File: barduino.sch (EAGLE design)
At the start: 14 parts, among them Q2 16MHz, X1 MINI-USB-UX60A-MB-5ST

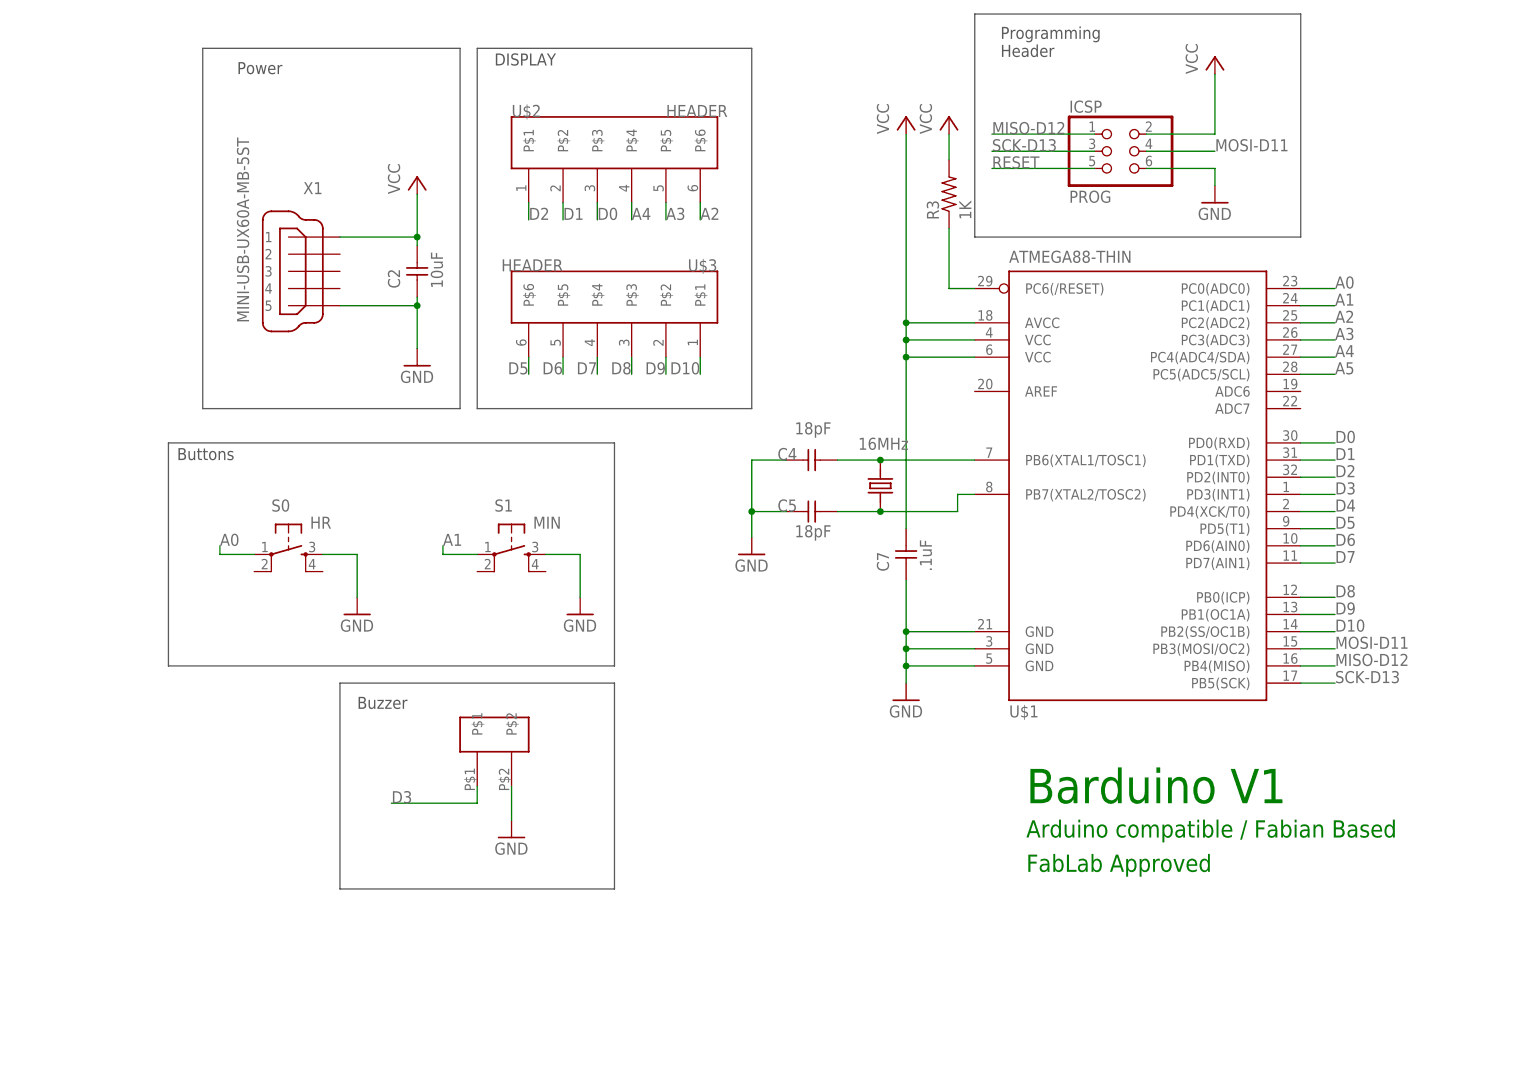
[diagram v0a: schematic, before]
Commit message: add current limiting resistors to the 4 digits
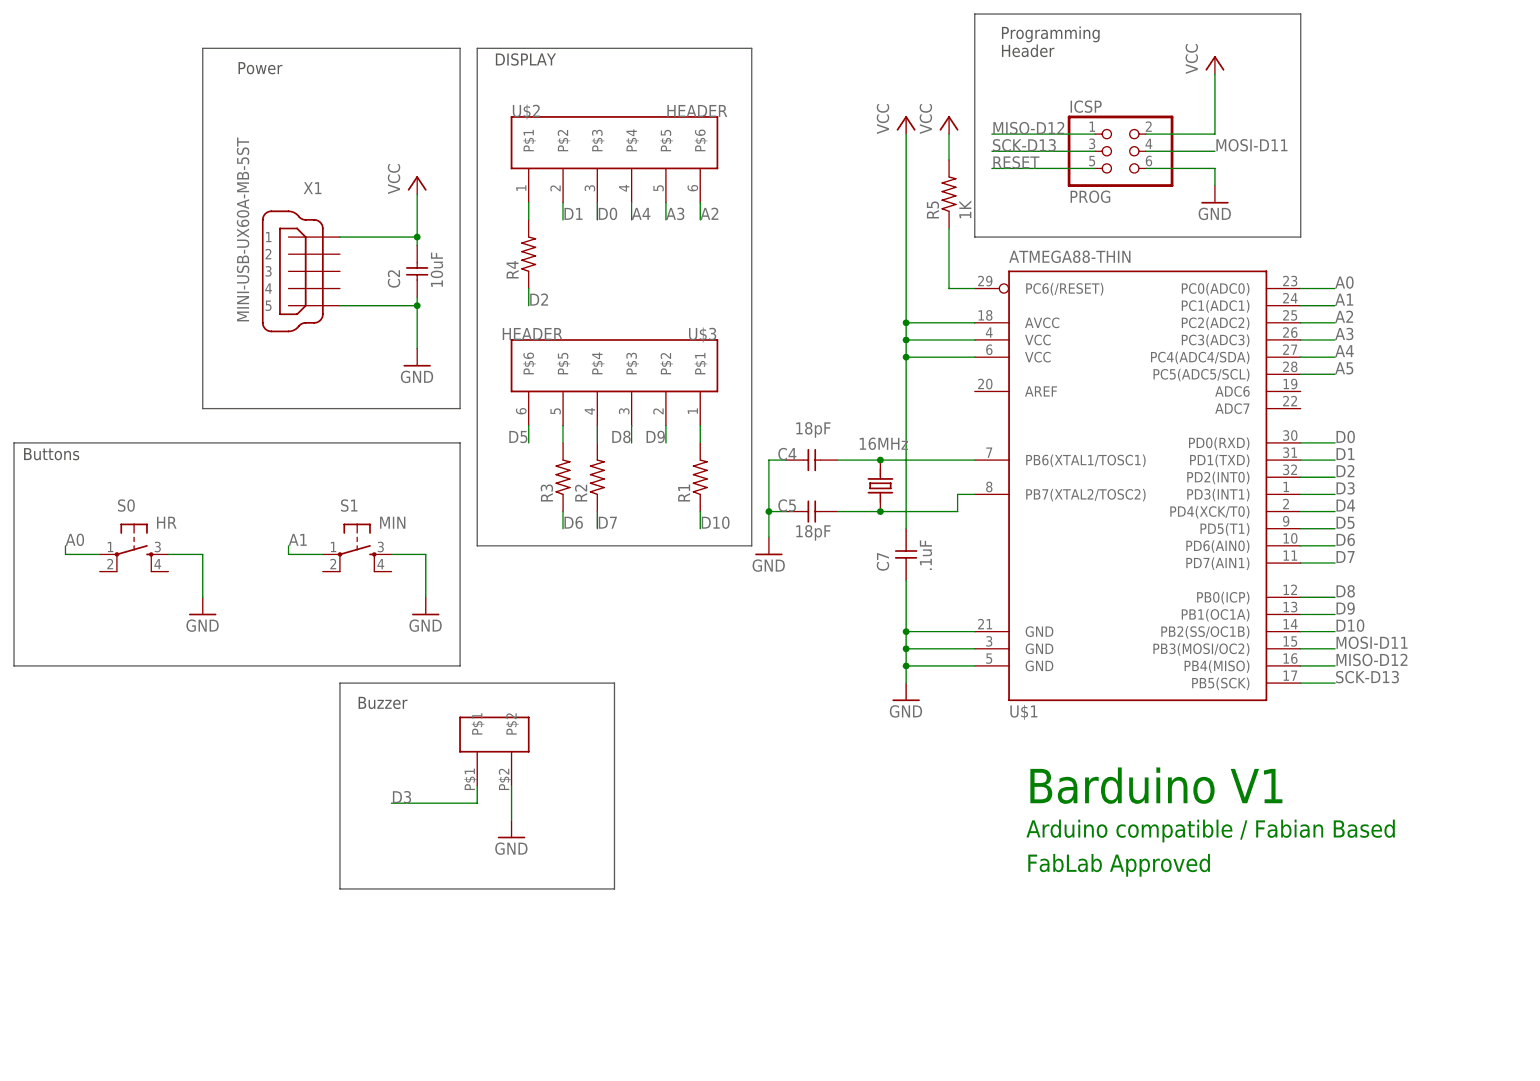
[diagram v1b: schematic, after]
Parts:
- added R1, R2, R4: (no value), resistor:R-US_R1206
- added R5: 1K, ng:RESISTOR1206
- R3: value 1K -> (none); device ng:RESISTOR1206 -> resistor:R-US_R1206
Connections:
- new net N$1: R1.2, U$3.P$1
- new net N$2: R2.2, U$3.P$4
- new net N$3: R3.2, U$3.P$5
- new net N$4: R4.2, U$2.P$1
- net D10: now also R1.1; no longer U$3.P$1
- net D2: now also R4.1; no longer U$2.P$1
- net D6: now also R3.1; no longer U$3.P$5
- net D7: now also R2.1; no longer U$3.P$4
- net RESET: now also R5.1; no longer R3.1
- net VCC: now also R5.2; no longer R3.2
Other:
- moved on the sheet: R3, S0, S1, U$3

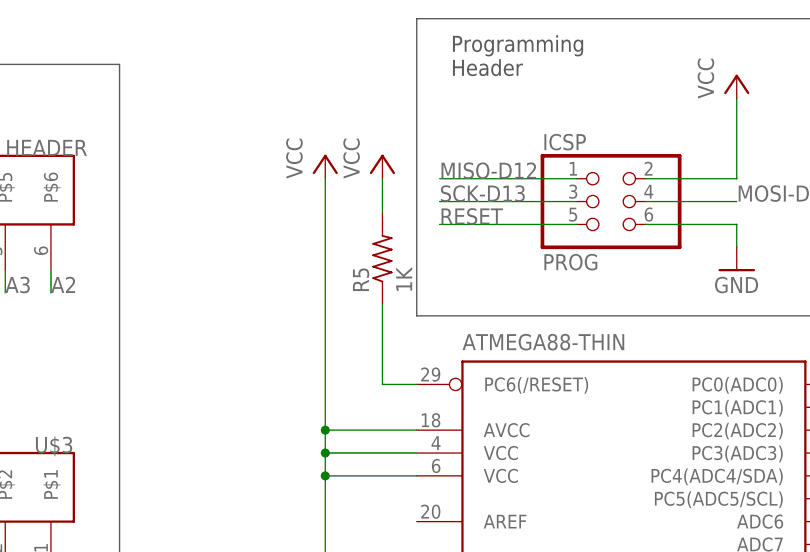
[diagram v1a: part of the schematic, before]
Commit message: reset pullup resistor should be 10k
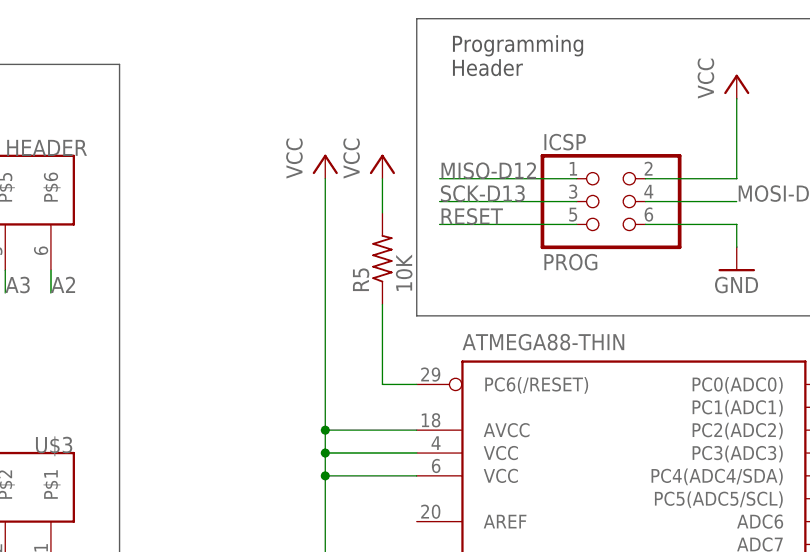
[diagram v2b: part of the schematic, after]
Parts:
- R5: value 1K -> 10K
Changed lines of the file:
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@@
 <part name="C4" library="ng" deviceset="UNPOLARIZED_CAPACITOR" device="1206" value="18pF"/>
 <part name="C5" library="ng" deviceset="UNPOLARIZED_CAPACITOR" device="1206" value="18pF"/>
-<part name="R5" library="ng" deviceset="RESISTOR" device="1206" value="1K"/>
+<part name="R5" library="ng" deviceset="RESISTOR" device="1206" value="10K"/>
 <part name="P+2" library="supply1" deviceset="VCC" device=""/>
 <part name="S0" library="ng" deviceset="6MM_SWITCH" device="6MM_SWITCH" value="HR"/>

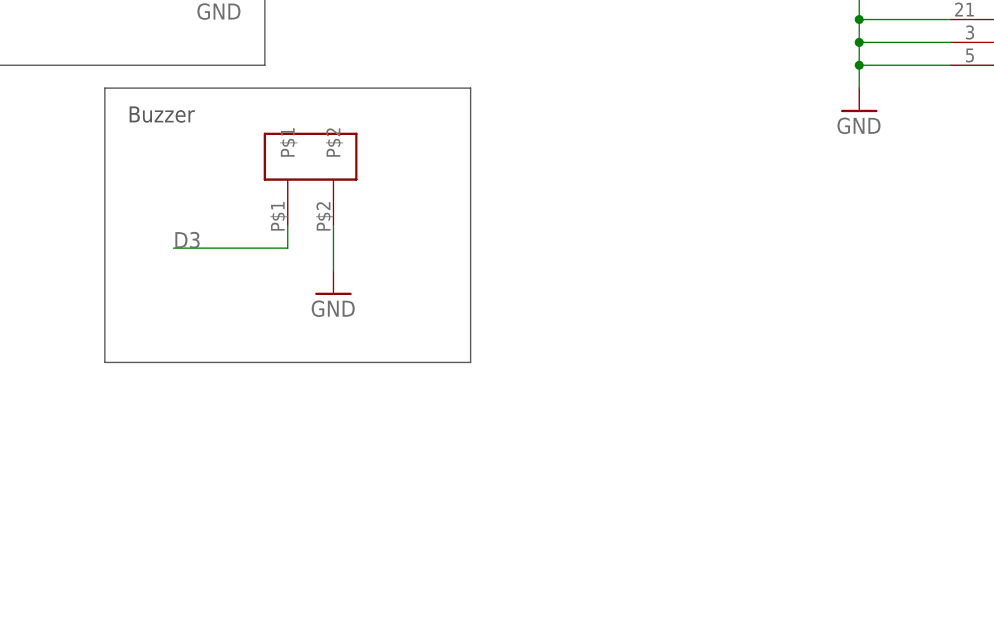
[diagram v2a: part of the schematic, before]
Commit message: add new 1206 AM and PM LEDs
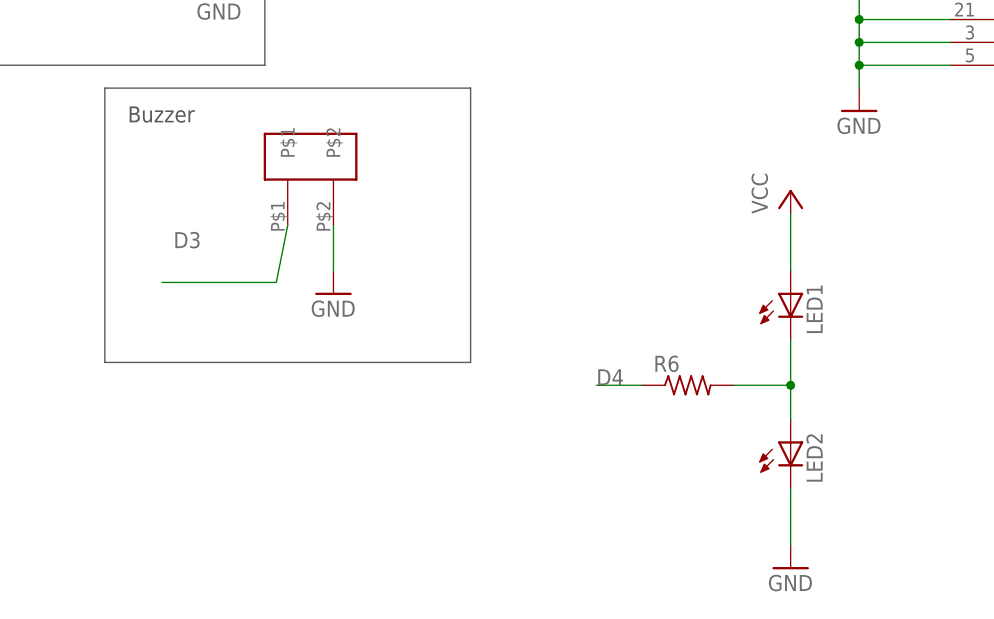
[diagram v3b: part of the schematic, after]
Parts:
- added LED1, LED2: (no value), led:LEDCHIPLED_1206
- added R6: (no value), resistor:R-US_R1206
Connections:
- new net N$5: LED1.C, LED2.A, R6.2
- net D4: now also R6.1
- net GND: now also LED2.C
- net VCC: now also LED1.A
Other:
- note added: "D4"
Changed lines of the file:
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@@
 <?xml version="1.0" encoding="utf-8"?>
 <!DOCTYPE eagle SYSTEM "eagle.dtd">
-<eagle version="8.2.1">
+<eagle version="8.2.2">
 <drawing>
 <settings>
@@
 <setting verticaltext="up"/>
 </settings>
-<grid distance="0.1" unitdist="inch" unit="inch" style="lines" multiple="1" display="no" altdistance="0.01" altunitdist="inch" altunit="inch"/>
+<grid distance="0.05" unitdist="inch" unit="inch" style="lines" multiple="1" display="no" altdistance="0.01" altunitdist="inch" altunit="inch"/>
 <layers>
 <layer number="1" name="Top" color="4" fill="1" visible="no" active="no"/>
@@
 <part name="R3" library="resistor" deviceset="R-US_" device="R1206"/>
 <part name="R4" library="resistor" deviceset="R-US_" device="R1206"/>
+<part name="LED1" library="led" deviceset="LED" device="CHIPLED_1206"/>
+<part name="LED2" library="led" deviceset="LED" device="CHIPLED_1206"/>
+<part name="P+5" library="supply1" deviceset="VCC" device=""/>
+<part name="GND8" library="supply1" library_urn="urn:adsk.eagle:library:371" deviceset="GND" device=""/>
+<part name="R6" library="resistor" deviceset="R-US_" device="R1206"/>
 </parts>
 <sheets>
@@
 <wire x1="116.84" y1="104.14" x2="116.84" y2="137.16" width="0.1524" layer="97"/>
 <wire x1="116.84" y1="137.16" x2="68.58" y2="137.16" width="0.1524" layer="97"/>
+<text x="29.21" y="5.08" size="1.778" layer="95">D4</text>
 </plain>
 <instances>
@@
 <instance part="R3" gate="G$1" x="7.62" y="68.58" rot="R90"/>
 <instance part="R4" gate="G$1" x="2.54" y="101.6" rot="R90"/>
+<instance part="LED1" gate="G$1" x="50.8" y="15.24"/>
+<instance part="LED2" gate="G$1" x="50.8" y="-1.27"/>
+<instance part="P+5" gate="VCC" x="50.8" y="26.67"/>
+<instance part="GND8" gate="1" x="50.8" y="-15.24"/>
+<instance part="R6" gate="G$1" x="39.37" y="5.08"/>
 </instances>
 <busses>
@@
 <pinref part="P+1" gate="VCC" pin="VCC"/>
 </segment>
+<segment>
+<wire x1="50.8" y1="24.13" x2="50.8" y2="17.78" width="0.1524" layer="91"/>
+<pinref part="P+5" gate="VCC" pin="VCC"/>
+<pinref part="LED1" gate="G$1" pin="A"/>
+</segment>
 </net>
 <net name="GND" class="1">
@@
 <wire x1="0" y1="17.78" x2="0" y2="22.86" width="0.1524" layer="91"/>
 </segment>
+<segment>
+<pinref part="GND8" gate="1" pin="GND"/>
+<wire x1="50.8" y1="-12.7" x2="50.8" y2="-6.35" width="0.1524" layer="91"/>
+<pinref part="LED2" gate="G$1" pin="C"/>
+</segment>
 </net>
 <net name="PB7" class="0">
@@
 <segment>
 <pinref part="U$4" gate="G$1" pin="P$1"/>
-<wire x1="-5.08" y1="22.86" x2="-5.08" y2="20.32" width="0.1524" layer="91"/>
-<wire x1="-5.08" y1="20.32" x2="-17.78" y2="20.32" width="0.1524" layer="91"/>
+<wire x1="-5.08" y1="22.86" x2="-6.35" y2="16.51" width="0.1524" layer="91"/>
+<wire x1="-6.35" y1="16.51" x2="-19.05" y2="16.51" width="0.1524" layer="91"/>
 <label x="-17.78" y="20.32" size="1.778" layer="95"/>
 </segment>
@@
 <label x="121.92" y="63.5" size="1.778" layer="95"/>
 <pinref part="U$1" gate="G$1" pin="PD4(XCK/T0)"/>
+</segment>
+<segment>
+<pinref part="R6" gate="G$1" pin="1"/>
+<wire x1="34.29" y1="5.08" x2="29.21" y2="5.08" width="0.1524" layer="91"/>
 </segment>
 </net>
@@
 </segment>
 </net>
+<net name="N$5" class="0">
+<segment>
+<pinref part="LED2" gate="G$1" pin="A"/>
+<wire x1="50.8" y1="1.27" x2="50.8" y2="5.08" width="0.1524" layer="91"/>
+<pinref part="LED1" gate="G$1" pin="C"/>
+<pinref part="R6" gate="G$1" pin="2"/>
+<wire x1="50.8" y1="5.08" x2="50.8" y2="10.16" width="0.1524" layer="91"/>
+<wire x1="44.45" y1="5.08" x2="50.8" y2="5.08" width="0.1524" layer="91"/>
+<junction x="50.8" y="5.08"/>
+</segment>
+</net>
